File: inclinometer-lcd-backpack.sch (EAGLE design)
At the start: 15 parts, among them IC1 ATmega328-DIP-Prgrammed, Q1 2N3904, U1 LCD-16X2NOHOLES, Y1 16MHz

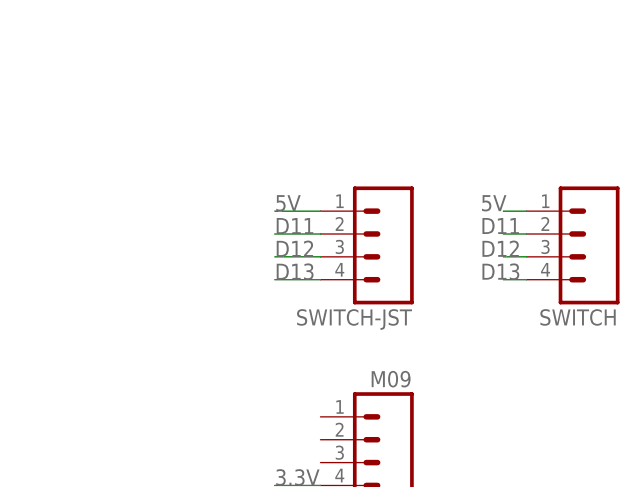
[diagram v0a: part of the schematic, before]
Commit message: Changes 3-way switch from 5V to GND, beefs up power connections to 0.016 wire width
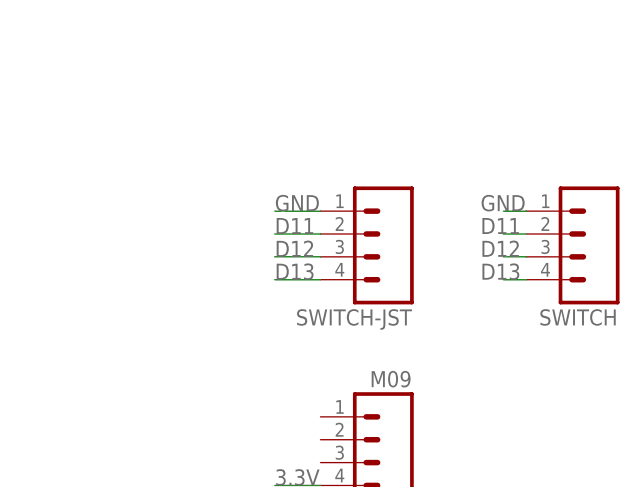
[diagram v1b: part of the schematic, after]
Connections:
- net 5V: no longer SWITCH-JST.1, SWITCH.1
- net GND: now also SWITCH-JST.1, SWITCH.1
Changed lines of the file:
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@@
-</segment>
-<segment>
-<pinref part="SWITCH-JST" gate="G$1" pin="1"/>
-<wire x1="198.12" y1="139.7" x2="193.04" y2="139.7" width="0.1524" layer="91"/>
-<label x="193.04" y="139.7" size="1.778" layer="95"/>
 </segment>
 <segment>
@@
 <pinref part="IC1" gate="G$1" pin="PC6(/RESET)"/>
 <pinref part="U$5" gate="G$1" pin="5V"/>
-</segment>
-<segment>
-<pinref part="SWITCH" gate="G$1" pin="1"/>
-<wire x1="218.44" y1="139.7" x2="220.98" y2="139.7" width="0.1524" layer="91"/>
-<label x="215.9" y="139.7" size="1.778" layer="95"/>
 </segment>
 </net>
@@
 <label x="193.04" y="99.06" size="1.778" layer="95"/>
 </segment>
+<segment>
+<pinref part="SWITCH-JST" gate="G$1" pin="1"/>
+<wire x1="198.12" y1="139.7" x2="193.04" y2="139.7" width="0.1524" layer="91"/>
+<label x="193.04" y="139.7" size="1.778" layer="95"/>
+</segment>
+<segment>
+<pinref part="SWITCH" gate="G$1" pin="1"/>
+<wire x1="218.44" y1="139.7" x2="220.98" y2="139.7" width="0.1524" layer="91"/>
+<label x="215.9" y="139.7" size="1.778" layer="95"/>
+</segment>
 </net>

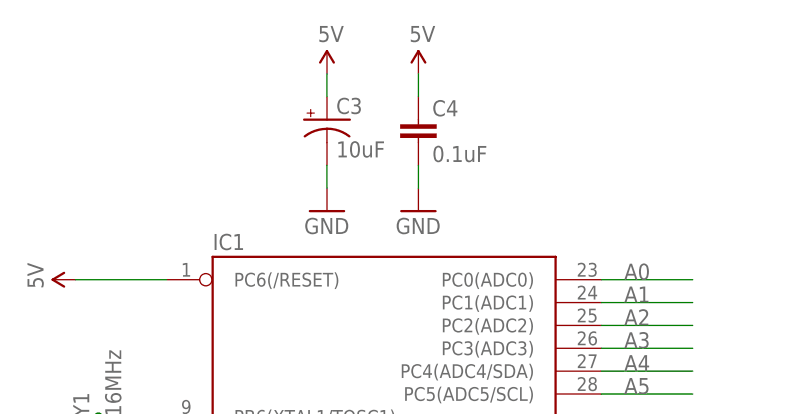
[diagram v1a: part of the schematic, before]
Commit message: Removes extra voltage smoothing caps (dual regulator board is doing this already)
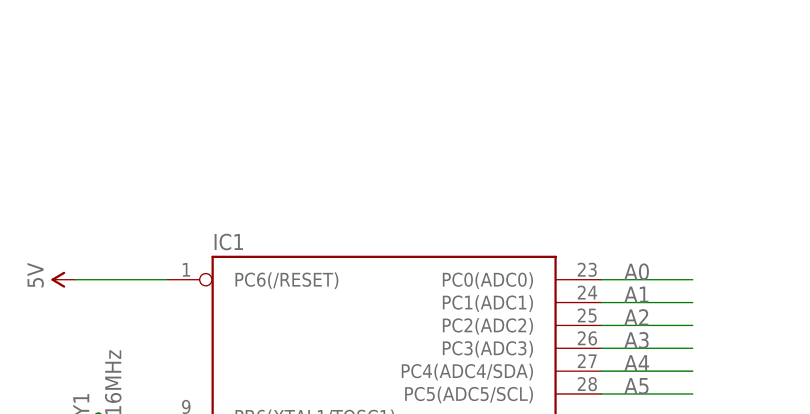
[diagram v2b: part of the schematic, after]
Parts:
- removed C3: 10uF, SparkFun:CAP_POLPTH2
- removed C4: 0.1uF, SparkFun:CAPPTH2
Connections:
- net 5V: no longer C3.+, C4.1
- net GND: no longer C3.-, C4.2
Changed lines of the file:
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@@
 <part name="GND3" library="SparkFun" deviceset="GND" device=""/>
 <part name="U$7" library="SparkFun" deviceset="5V" device=""/>
-<part name="C3" library="SparkFun" deviceset="CAP_POL" device="PTH2" value="10uF"/>
-<part name="U$8" library="SparkFun" deviceset="5V" device=""/>
-<part name="GND2" library="SparkFun" deviceset="GND" device=""/>
 <part name="GND4" library="SparkFun" deviceset="GND" device=""/>
-<part name="C4" library="SparkFun" deviceset="CAP" device="PTH2" value="0.1uF"/>
-<part name="U$9" library="SparkFun" deviceset="5V" device=""/>
-<part name="GND5" library="SparkFun" deviceset="GND" device=""/>
 <part name="U1" library="SparkFun-Displays" deviceset="LCD-16X2" device="NOHOLES" value="LCD-16X2NOHOLES"/>
 <part name="GND6" library="SparkFun" deviceset="GND" device=""/>
@@
 <instance part="GND3" gate="1" x="86.36" y="93.98"/>
 <instance part="U$7" gate="G$1" x="27.94" y="152.4"/>
-<instance part="C3" gate="G$1" x="119.38" y="149.86"/>
-<instance part="U$8" gate="G$1" x="119.38" y="154.94"/>
-<instance part="GND2" gate="1" x="119.38" y="139.7"/>
 <instance part="GND4" gate="1" x="27.94" y="137.16"/>
-<instance part="C4" gate="G$1" x="129.54" y="147.32"/>
-<instance part="U$9" gate="G$1" x="129.54" y="154.94"/>
-<instance part="GND5" gate="1" x="129.54" y="139.7"/>
 <instance part="U1" gate="G$1" x="20.32" y="73.66" smashed="yes" rot="R180">
 <attribute name="NAME" x="27.94" y="50.292" size="1.778" layer="95" rot="R180"/>
@@
 <pinref part="U$6" gate="G$1" pin="5V"/>
 <pinref part="IC1" gate="G$1" pin="AVCC"/>
-</segment>
-<segment>
-<wire x1="119.38" y1="152.4" x2="119.38" y2="154.94" width="0.1524" layer="91"/>
-<pinref part="C3" gate="G$1" pin="+"/>
-<pinref part="U$8" gate="G$1" pin="5V"/>
-</segment>
-<segment>
-<wire x1="129.54" y1="152.4" x2="129.54" y2="154.94" width="0.1524" layer="91"/>
-<pinref part="C4" gate="G$1" pin="1"/>
-<pinref part="U$9" gate="G$1" pin="5V"/>
 </segment>
 <segment>
@@
 </segment>
 <segment>
-<wire x1="119.38" y1="142.24" x2="119.38" y2="144.78" width="0.1524" layer="91"/>
-<pinref part="GND2" gate="1" pin="GND"/>
-<pinref part="C3" gate="G$1" pin="-"/>
-</segment>
-<segment>
-<wire x1="129.54" y1="142.24" x2="129.54" y2="144.78" width="0.1524" layer="91"/>
-<pinref part="GND5" gate="1" pin="GND"/>
-<pinref part="C4" gate="G$1" pin="2"/>
-</segment>
-<segment>

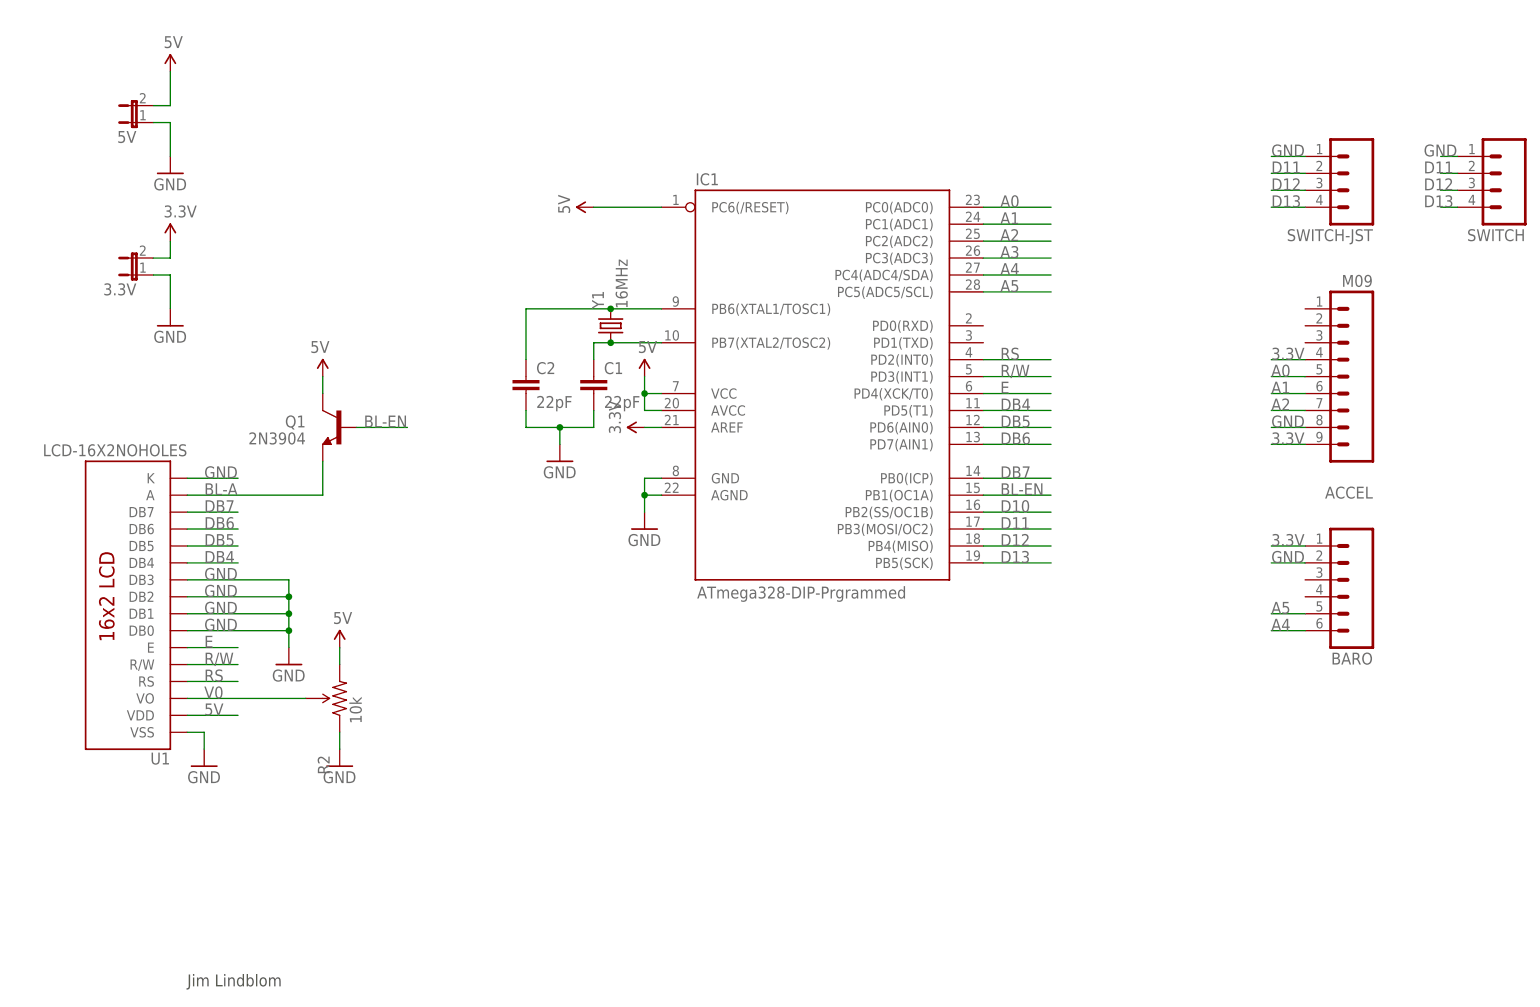
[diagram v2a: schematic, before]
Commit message: Switches to 10DOF board from Sunkee
http://www.amazon.com/gp/product/B00CD239UG/ref=oh_details_o01_s00_i00?ie=UTF8&psc=1
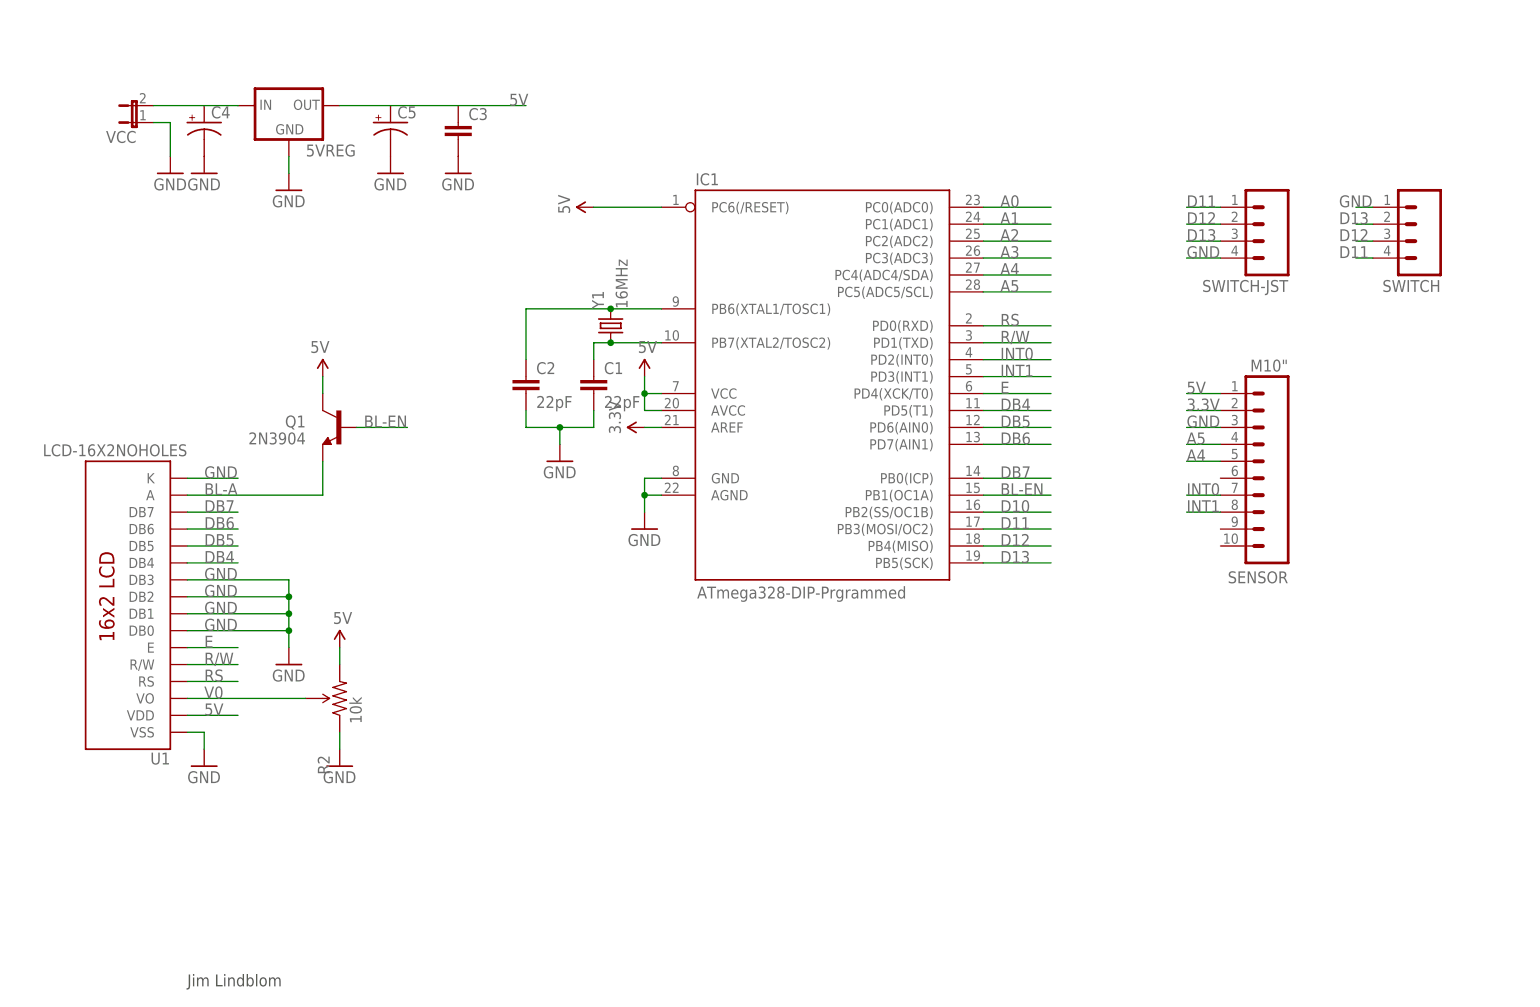
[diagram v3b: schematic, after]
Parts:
- removed 3.3V: (no value), SparkFun-Passives:JUMPER-2PTH
- removed ACCEL: M09, SparkFun-Connectors:M09
- removed BARO: (no value), SparkFun:M06SIP
- added 5VREG: (no value), v-reg:78XXS
- added C3: (no value), SparkFun-Capacitors:CAPPTH2
- added C4, C5: (no value), SparkFun-Capacitors:CAP_POLPTH2
- added SENSOR: M10", SparkFun-Connectors:M10"
- renumbered 5V to VCC
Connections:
- new net INT0: IC1.PD2(INT0), SENSOR.7
- new net INT1: IC1.PD3(INT1), SENSOR.8
- new net VCC: 5VREG.IN, C4.+, VCC.2
- net 3.3V: now also SENSOR.2; no longer 3.3V.2, ACCEL.4, ACCEL.9, BARO.1
- net 5V: now also 5VREG.OUT, C3.1, C5.+, SENSOR.1; no longer VCC.2
- net A0: no longer ACCEL.5
- net A1: no longer ACCEL.6
- net A2: no longer ACCEL.7
- net A4: now also SENSOR.5; no longer BARO.6
- net A5: now also SENSOR.4; no longer BARO.5
- net D11: now also SWITCH-JST.1, SWITCH.4; no longer SWITCH-JST.2, SWITCH.2
- net D12: now also SWITCH-JST.2; no longer SWITCH-JST.3
- net D13: now also SWITCH-JST.3, SWITCH.2; no longer SWITCH-JST.4, SWITCH.4
- net GND: now also 5VREG.GND, C3.2, C4.-, C5.-, SENSOR.3, SWITCH-JST.4; no longer 3.3V.1, ACCEL.8, BARO.2, SWITCH-JST.1
- net R/W: now also IC1.PD1(TXD); no longer IC1.PD3(INT1)
- net RS: now also IC1.PD0(RXD); no longer IC1.PD2(INT0)
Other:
- moved on the sheet: SWITCH, SWITCH-JST

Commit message: Adds screw terminals, connects currently unused pins
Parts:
- removed VCC: (no value), SparkFun-Passives:JUMPER-2PTH
- added JP1: M025MM, SparkFun-Connectors:M025MM
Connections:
- net A1: now also SENSOR.10
- net A2: now also SENSOR.9
- net A3: now also SENSOR.6
- net GND: now also JP1.1; no longer VCC.1
- net VCC: now also JP1.2; no longer VCC.2
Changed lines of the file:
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@@
 <part name="Q1" library="SparkFun" deviceset="TRANSISTOR_NPN" device="TO92" value="2N3904"/>
 <part name="U$3" library="SparkFun" deviceset="5V" device=""/>
-<part name="VCC" library="SparkFun-Passives" deviceset="JUMPER-2" device="PTH"/>
 <part name="U$10" library="SparkFun-Aesthetics" deviceset="3.3V" device=""/>
 <part name="R2" library="SparkFun-Electromechanical" deviceset="TRIMPOT" device="PTH" value="10k"/>
@@
 <part name="GND10" library="SparkFun" deviceset="GND" device=""/>
 <part name="SENSOR" library="SparkFun-Connectors" deviceset="M10" device="&quot;"/>
+<part name="JP1" library="SparkFun-Connectors" deviceset="M02" device="5MM"/>
 </parts>
 <sheets>
@@
 <instance part="Q1" gate="G$1" x="53.34" y="99.06" rot="MR0"/>
 <instance part="U$3" gate="G$1" x="50.8" y="106.68" rot="MR0"/>
-<instance part="VCC" gate="A" x="22.86" y="144.78" rot="R90"/>
 <instance part="U$10" gate="G$1" x="99.06" y="99.06" rot="R90"/>
 <instance part="R2" gate="R?" x="53.34" y="58.42" rot="R90"/>
@@
 <instance part="GND10" gate="1" x="71.12" y="137.16"/>
 <instance part="SENSOR" gate="G$1" x="195.58" y="86.36" rot="R180"/>
+<instance part="JP1" gate="G$1" x="17.78" y="144.78"/>
 </instances>
 <busses>
@@
 <wire x1="27.94" y1="144.78" x2="27.94" y2="139.7" width="0.1524" layer="91"/>
 <pinref part="GND4" gate="1" pin="GND"/>
-<pinref part="VCC" gate="A" pin="1"/>
+<pinref part="JP1" gate="G$1" pin="1"/>
 </segment>
 <segment>
@@
 <pinref part="IC1" gate="G$1" pin="PC1(ADC1)"/>
 </segment>
+<segment>
+<pinref part="SENSOR" gate="G$1" pin="10"/>
+<wire x1="185.42" y1="81.28" x2="180.34" y2="81.28" width="0.1524" layer="91"/>
+<label x="180.34" y="81.28" size="1.778" layer="95"/>
+</segment>
 </net>
 <net name="A2" class="0">
@@
 <pinref part="IC1" gate="G$1" pin="PC2(ADC2)"/>
 </segment>
+<segment>
+<pinref part="SENSOR" gate="G$1" pin="9"/>
+<wire x1="185.42" y1="83.82" x2="180.34" y2="83.82" width="0.1524" layer="91"/>
+<label x="180.34" y="83.82" size="1.778" layer="95"/>
+</segment>
 </net>
 <net name="A3" class="0">
@@
 <label x="152.4" y="124.46" size="1.778" layer="95"/>
 <pinref part="IC1" gate="G$1" pin="PC3(ADC3)"/>
+</segment>
+<segment>
+<pinref part="SENSOR" gate="G$1" pin="6"/>
+<wire x1="185.42" y1="91.44" x2="180.34" y2="91.44" width="0.1524" layer="91"/>
+<label x="180.34" y="91.44" size="1.778" layer="95"/>
 </segment>
 </net>
@@
 <segment>
 <wire x1="25.4" y1="147.32" x2="33.02" y2="147.32" width="0.1524" layer="91"/>
-<pinref part="VCC" gate="A" pin="2"/>
 <pinref part="C4" gate="G$1" pin="+"/>
 <pinref part="5VREG" gate="1" pin="IN"/>
 <wire x1="33.02" y1="147.32" x2="38.1" y2="147.32" width="0.1524" layer="91"/>
-</segment>
-</net>
+<pinref part="JP1" gate="G$1" pin="2"/>
+</segment>
+</net>

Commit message: Moves ATMEGA a tad so it's easier to remove, updates silkscreens on some pins
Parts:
- Q1: device SparkFun:TRANSISTOR_NPNTO92 -> SparkFun-DiscreteSemi:TRANSISTOR_NPNTO92
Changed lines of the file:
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@@
 <part name="GND7" library="SparkFun" deviceset="GND" device=""/>
 <part name="GND8" library="SparkFun" deviceset="GND" device=""/>
-<part name="Q1" library="SparkFun" deviceset="TRANSISTOR_NPN" device="TO92" value="2N3904"/>
+<part name="Q1" library="SparkFun-DiscreteSemi" deviceset="TRANSISTOR_NPN" device="TO92" value="2N3904"/>
 <part name="U$3" library="SparkFun" deviceset="5V" device=""/>
 <part name="U$10" library="SparkFun-Aesthetics" deviceset="3.3V" device=""/>
